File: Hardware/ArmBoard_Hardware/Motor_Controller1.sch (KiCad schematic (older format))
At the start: 13 parts

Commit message: added missing lables to connectors
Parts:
- MC1: symbol MRDT_ICs:VNH5019A_E -> ArmBoard_Hardware-rescue:VNH5019A_E-MRDT_ICs
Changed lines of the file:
@@
 $EndComp
 $Comp
-L MRDT_ICs:VNH5019A_E MC1
+L ArmBoard_Hardware-rescue:VNH5019A_E-MRDT_ICs MC1
 U 1 1 628AD5AB
 P 4925 4600

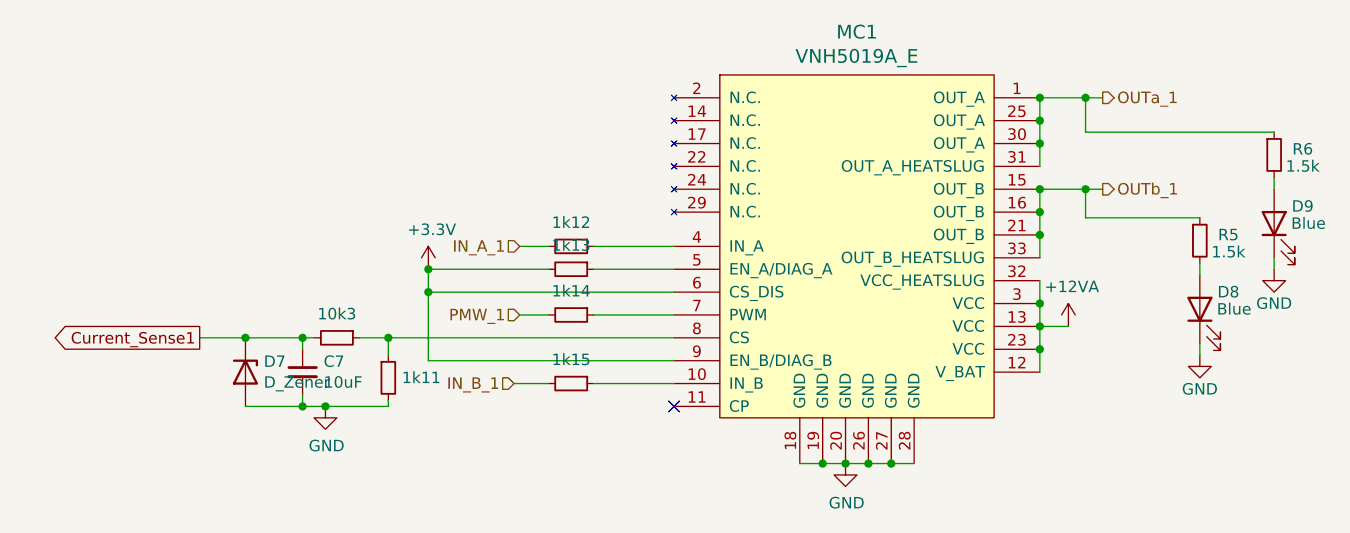
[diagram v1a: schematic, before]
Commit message: schematic changes, encoder changes, led changes
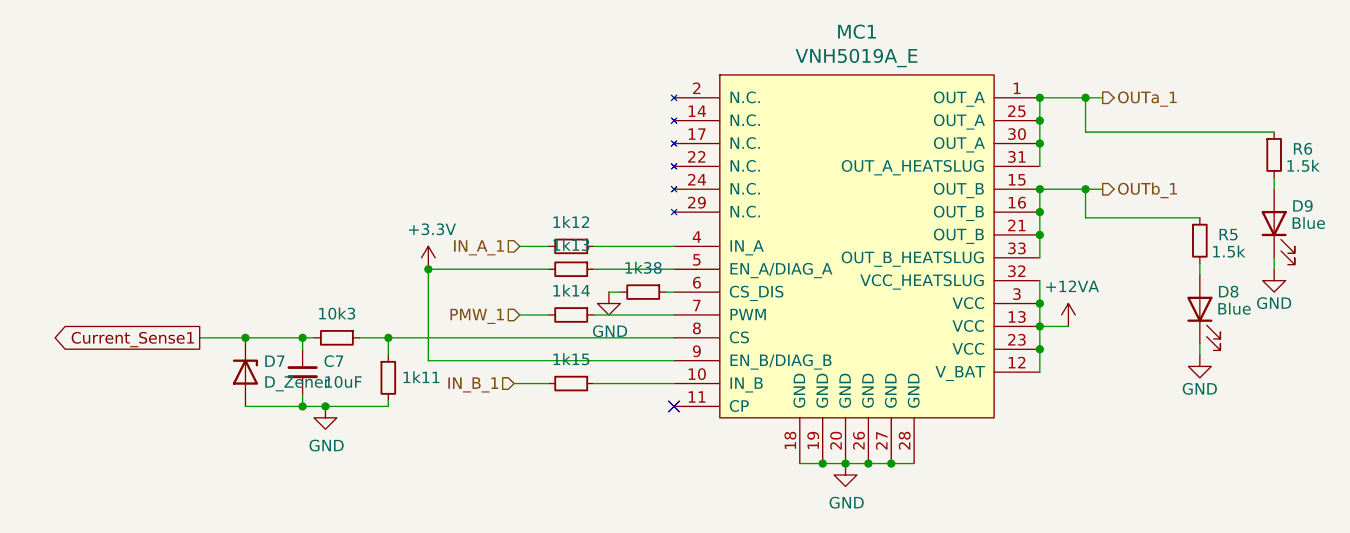
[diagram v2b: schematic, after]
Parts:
- added 1k38: R_Small, Resistor_SMD:R_0603_1608Metric_Pad0.98x0.95mm_HandSolder, symbol Device:R_Small
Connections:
- net +3V3: no longer MC1.6 (CS_DIS)
- net GND: now also 1k38.2
- new net: 1k38.1, MC1.6 (CS_DIS)
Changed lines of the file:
@@
 Wire Wire Line
 	4175 4150 4050 4150
-Wire Wire Line
-	4725 4050 3650 4050
-Wire Wire Line
-	3650 4050 3650 3950
 Connection ~ 3650 3950
 Wire Wire Line
 	4725 4350 3650 4350
-Wire Wire Line
-	3650 4350 3650 4050
-Connection ~ 3650 4050
 Wire Wire Line
 	4725 4250 3475 4250
@@
 Text HLabel 6600 3600 2    50   Output ~ 0
 OUTb_1
+Wire Wire Line
+	3650 3950 3650 4350
+$Comp
+L power:GND #PWR05
+U 1 1 6291DCD5
+P 4440 4050
+AR Path="/63845F20/6291DCD5" Ref="#PWR05"  Part="1"
+AR Path="/628CE14B/6291DCD5" Ref="#PWR?"  Part="1"
+AR Path="/6297969A/6291DCD5" Ref="#PWR?"  Part="1"
+AR Path="/629F46F6/6291DCD5" Ref="#PWR?"  Part="1"
+AR Path="/629F46FD/6291DCD5" Ref="#PWR?"  Part="1"
+AR Path="/62A5CC3B/6291DCD5" Ref="#PWR?"  Part="1"
+AR Path="/62A5CC46/6291DCD5" Ref="#PWR?"  Part="1"
+AR Path="/62AF9C52/6291DCD5" Ref="#PWR?"  Part="1"
+AR Path="/62D2CE1B/6291DCD5" Ref="#PWR?"  Part="1"
+F 0 "#PWR05" H 4440 3800 50  0001 C CNN
+F 1 "GND" H 4445 3877 50  0000 C CNN
+F 2 "" H 4440 4050 50  0001 C CNN
+F 3 "" H 4440 4050 50  0001 C CNN
+	1    4440 4050
+	1    0    0    -1
+$EndComp
+$Comp
+L Device:R_Small 1k38
+U 1 1 6291DCDB
+P 4590 4050
+AR Path="/63845F20/6291DCDB" Ref="1k38"  Part="1"
+AR Path="/628CE14B/6291DCDB" Ref="1k?"  Part="1"
+AR Path="/6297969A/6291DCDB" Ref="1k?"  Part="1"
+AR Path="/629F46F6/6291DCDB" Ref="1k?"  Part="1"
+AR Path="/629F46FD/6291DCDB" Ref="1k?"  Part="1"
+AR Path="/62A5CC3B/6291DCDB" Ref="1k?"  Part="1"
+AR Path="/62A5CC46/6291DCDB" Ref="1k?"  Part="1"
+AR Path="/62AF9C52/6291DCDB" Ref="1k?"  Part="1"
+AR Path="/62C19165/6291DCDB" Ref="1k?"  Part="1"
+AR Path="/62CA8FD7/6291DCDB" Ref="1k?"  Part="1"
+AR Path="/62CBA1AC/6291DCDB" Ref="1k?"  Part="1"
+AR Path="/62CCE879/6291DCDB" Ref="1k?"  Part="1"
+AR Path="/62CE0B38/6291DCDB" Ref="1k?"  Part="1"
+AR Path="/62CF1227/6291DCDB" Ref="1k?"  Part="1"
+AR Path="/62D0C672/6291DCDB" Ref="1k?"  Part="1"
+AR Path="/62D1BEB1/6291DCDB" Ref="1k?"  Part="1"
+AR Path="/62D2CE1B/6291DCDB" Ref="1k?"  Part="1"
+AR Path="/62D3BCB9/6291DCDB" Ref="1k?"  Part="1"
+AR Path="/62D4BAA1/6291DCDB" Ref="1k?"  Part="1"
+F 0 "1k38" V 4486 4050 50  0000 C CNN
+F 1 "R_Small" V 4485 4050 50  0001 C CNN
+F 2 "Resistor_SMD:R_0603_1608Metric_Pad0.98x0.95mm_HandSolder" H 4590 4050 50  0001 C CNN
+F 3 "~" H 4590 4050 50  0001 C CNN
+	1    4590 4050
+	0    1    1    0
+$EndComp
+Wire Wire Line
+	4440 4050 4490 4050
+Wire Wire Line
+	4690 4050 4725 4050
 $EndSCHEMATC

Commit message: gerbs added and zipped
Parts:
- MC1: symbol ArmBoard_Hardware-rescue:VNH5019A_E-MRDT_ICs -> MRDT_ICs:VNH5019A_E
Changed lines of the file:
@@
 $EndComp
 $Comp
-L ArmBoard_Hardware-rescue:VNH5019A_E-MRDT_ICs MC1
+L MRDT_ICs:VNH5019A_E MC1
 U 1 1 628AD5AB
 P 4925 4600
